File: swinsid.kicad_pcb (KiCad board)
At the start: 2 copper layers, 17.5 x 36.6 mm, 16 parts, among them J1 Conn_PIC_ICSP_ICD, U1 ATmega88PA-AU, U2 SID6581, X1 SG-7050CAN

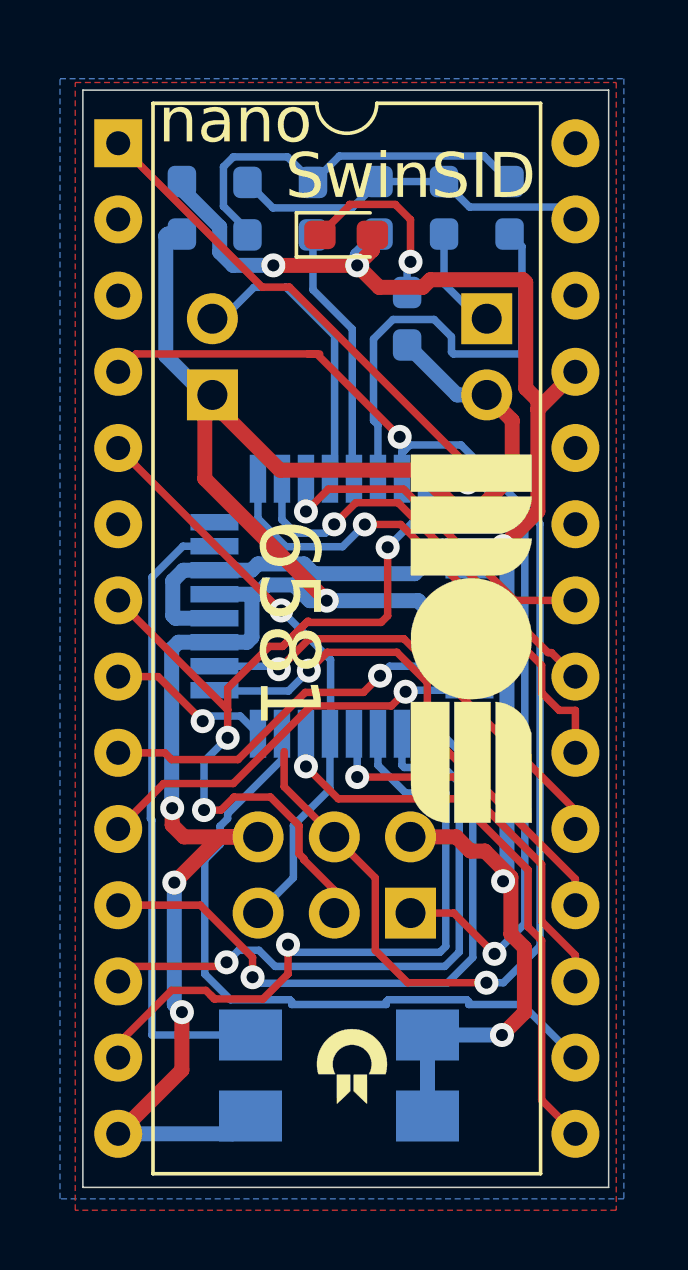
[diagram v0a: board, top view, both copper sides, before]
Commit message: New layout without C logo Remove ICSP 2x3 header for better layout Rotate MCU for better layout
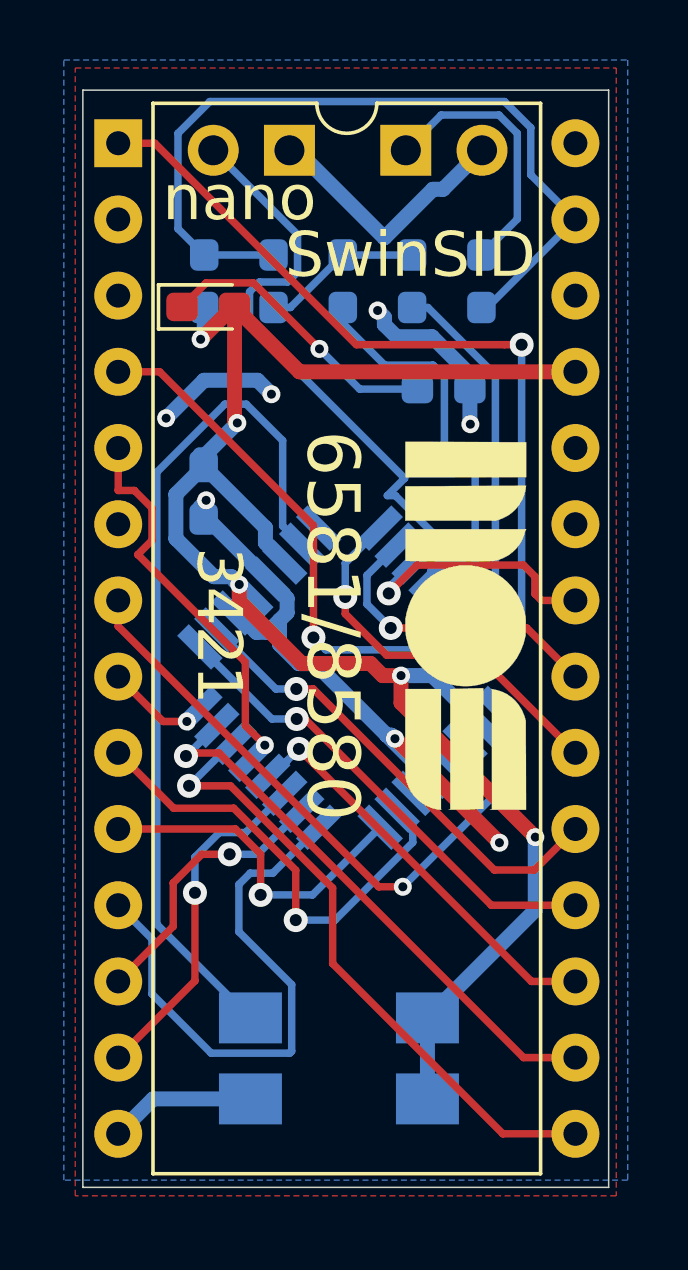
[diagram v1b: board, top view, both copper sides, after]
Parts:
- removed the G*** at (128.6, 76.0)
- removed J1: Conn_PIC_ICSP_ICD, Connector_PinHeader_2.54mm:PinHeader_2x03_P2.54mm_Vertical
- moved C1 9.53 mm to (123.7, 56.9)
- moved JP1 8.55 mm to (126.5, 45.4), turned to 90 degrees
- moved R3 6.30 mm to (123.7, 49.8)
- moved JP2 6.23 mm to (130.4, 45.4), turned to 270 degrees
- moved D1 5.18 mm to (123.8, 50.7)
- moved R5 4.07 mm to (130.6, 49.8)
- moved R4 2.75 mm to (132.9, 49.8), turned to 90 degrees
- moved R6 2.64 mm to (131.7, 53.4), turned to 0 degrees
- moved R2 2.62 mm to (128.3, 49.8)
- moved R1 2.57 mm to (126.0, 49.8)
- moved U1 2.40 mm to (128.5, 63.0), turned to 315 degrees
- moved X1 0.57 mm to (128.2, 75.7)
- moved G*** 0.47 mm to (132.4, 61.3)
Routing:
- net MOSI: track 47.6 -> 18.4 mm, vias 2 -> 1
- net GND: track 73.3 -> 44.3 mm, vias 5 -> 7
- net Net-(R1-Pad1): track 12.4 -> 27.3 mm
- net MISO: track 40.1 -> 26.8 mm, vias 2 -> 1
- net A3: track 21.1 -> 9.33 mm
- net A4: track 22.7 -> 11.6 mm
- net SELECT: track 10.5 -> 20.2 mm
- net +5V: track 67.6 -> 59.4 mm
- net Net-(R1-Pad2): track 13.4 -> 5.35 mm
- net RW: track 29.6 -> 21.7 mm, vias 3 -> 1
- net XTAL1: track 21.1 -> 28.9 mm
- net RESET: track 19.4 -> 12.6 mm
- net Net-(JP2-Pad1): track 3.41 -> 9.00 mm
- net D5: track 17.9 -> 12.9 mm
- net AUDIO1: track 8.44 -> 12.8 mm
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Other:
- board text added: "3421"
- board text added: "6581/8580"
- board text added: "Sck"
- board text removed: "6581"
- board text removed: "Rw"

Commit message: Updated swinsid image
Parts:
- removed G***: LOGO, custom:mosBig
